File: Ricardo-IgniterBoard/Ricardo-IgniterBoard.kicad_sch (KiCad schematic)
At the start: 39 parts, among them J101 RBUS, U101 ESP32-S3, Y101 R940000171

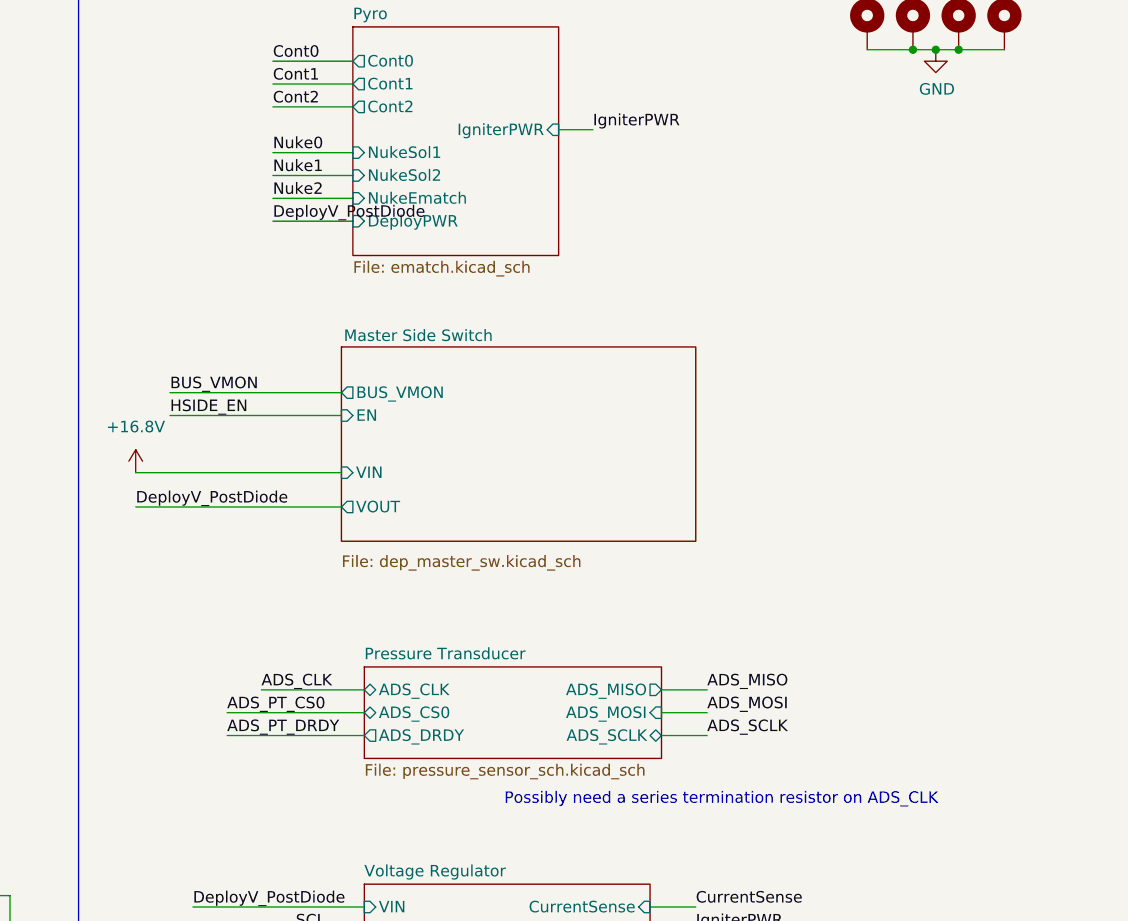
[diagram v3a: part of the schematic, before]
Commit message: some more changes
added current sensor for solenoid, fixed optocouplers
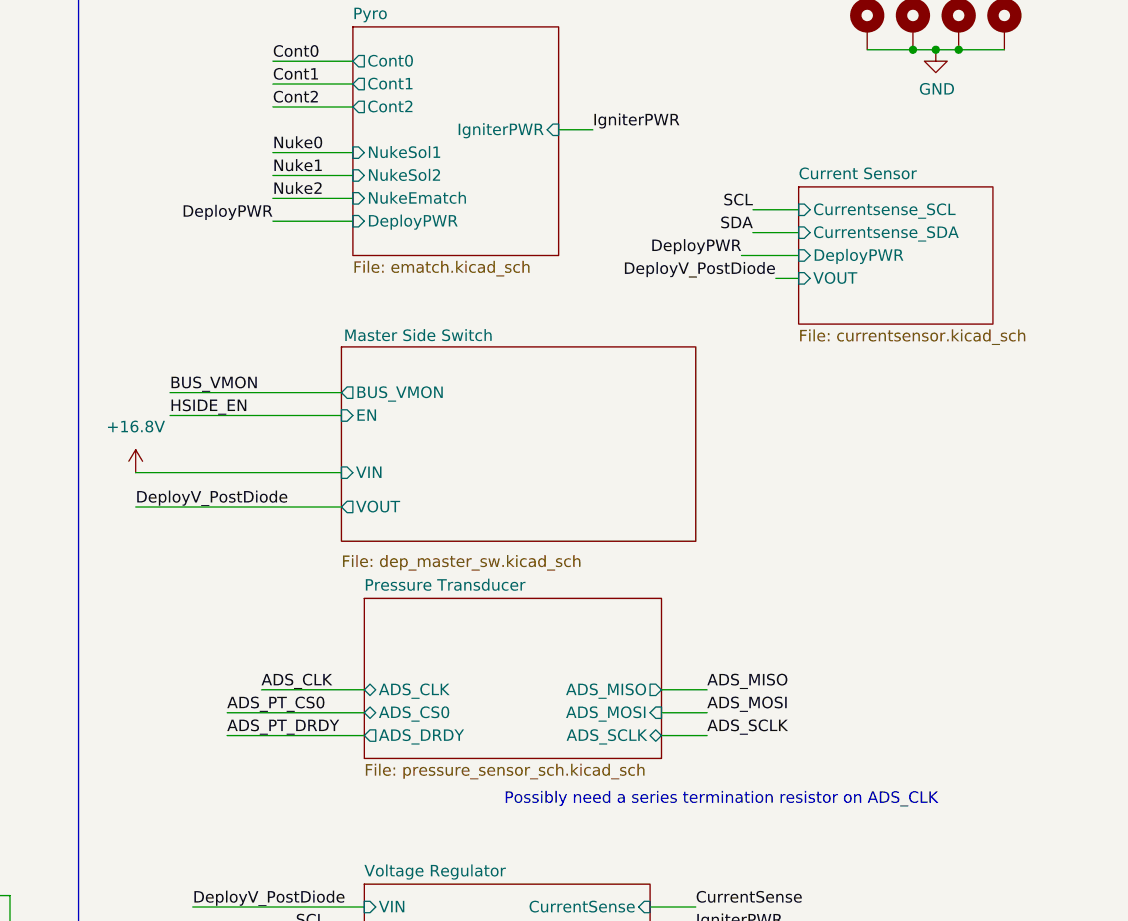
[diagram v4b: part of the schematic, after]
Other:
- added sheet Current Sensor (currentsensor.kicad_sch)
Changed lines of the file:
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@@
 	(wire
 		(pts
+			(xy 248.92 55.88) (xy 255.27 55.88)
+		)
+		(stroke
+			(width 0)
+			(type default)
+		)
+	)
+	(wire
+		(pts
 			(xy 69.85 135.89) (xy 69.85 138.43)
 		)
@@
 	(wire
 		(pts
+			(xy 250.19 50.8) (xy 255.27 50.8)
+		)
+		(stroke
+			(width 0)
+			(type default)
+		)
+	)
+	(wire
+		(pts
 			(xy 242.57 149.86) (xy 247.65 149.86)
 		)
@@
 	(wire
 		(pts
+			(xy 250.19 53.34) (xy 255.27 53.34)
+		)
+		(stroke
+			(width 0)
+			(type default)
+		)
+	)
+	(wire
+		(pts
 			(xy 196.85 46.99) (xy 205.74 46.99)
 		)
@@
 	(wire
 		(pts
+			(xy 252.73 58.42) (xy 255.27 58.42)
+		)
+		(stroke
+			(width 0)
+			(type default)
+		)
+	)
+	(wire
+		(pts
 			(xy 26.67 165.1) (xy 34.29 165.1)
 		)
@@
 		)
 	)
+	(label "DeployPWR"
+		(at 196.85 52.07 180)
+		(effects
+			(font
+				(size 1.27 1.27)
+			)
+			(justify right bottom)
+		)
+	)
 	(label "SDA"
 		(at 52.07 97.79 0)
@@
 		)
 	)
+	(label "SDA"
+		(at 250.19 53.34 180)
+		(effects
+			(font
+				(size 1.27 1.27)
+			)
+			(justify right bottom)
+		)
+	)
 	(label "Nuke2"
 		(at 196.85 49.53 0)
@@
 		)
 	)
+	(label "DeployPWR"
+		(at 248.92 55.88 180)
+		(effects
+			(font
+				(size 1.27 1.27)
+			)
+			(justify right bottom)
+		)
+	)
 	(label "ADS_PT_CS0"
 		(at 66.04 95.25 180)
@@
 		)
 	)
+	(label "DeployV_PostDiode"
+		(at 252.73 58.42 180)
+		(effects
+			(font
+				(size 1.27 1.27)
+			)
+			(justify right bottom)
+		)
+	)
 	(label "IgniterPWR"
 		(at 232.41 41.91 0)
@@
 		)
 	)
+	(label "SCL"
+		(at 250.19 50.8 180)
+		(effects
+			(font
+				(size 1.27 1.27)
+			)
+			(justify right bottom)
+		)
+	)
 	(label "ADS_MISO"
 		(at 245.11 104.14 0)
@@
 		)
 	)
-	(label "DeployV_PostDiode"
-		(at 196.85 52.07 0)
-		(effects
-			(font
-				(size 1.27 1.27)
-			)
-			(justify left bottom)
-		)
-	)
 	(label "Nuke1"
 		(at 138.43 97.79 0)
@@
 	)
 	(sheet
-		(at 207.01 101.6)
-		(size 33.02 10.16)
+		(at 255.27 48.26)
+		(size 21.59 15.24)
+		(exclude_from_sim no)
+		(in_bom yes)
+		(on_board yes)
+		(dnp no)
+		(fields_autoplaced yes)
+		(stroke
+			(width 0.1524)
+			(type solid)
+		)
+		(fill
+			(color 0 0 0 0.0000)
+		)
+		(property "Sheetname" "Current Sensor"
+			(at 255.27 47.5484 0)
+			(effects
+				(font
+					(size 1.27 1.27)
+				)
+				(justify left bottom)
+			)
+		)
+		(property "Sheetfile" "currentsensor.kicad_sch"
+			(at 255.27 64.0846 0)
+			(effects
+				(font
+					(size 1.27 1.27)
+				)
+				(justify left top)
+			)
+		)
+		(pin "Currentsense_SCL" input
+			(at 255.27 50.8 180)
+			(effects
+				(font
+					(size 1.27 1.27)
+				)
+				(justify left)
+			)
+		)
+		(pin "Currentsense_SDA" input
+			(at 255.27 53.34 180)
+			(effects
+				(font
+					(size 1.27 1.27)
+				)
+				(justify left)
+			)
+		)
+		(pin "DeployPWR" input
+			(at 255.27 55.88 180)
+			(effects
+				(font
+					(size 1.27 1.27)
+				)
+				(justify left)
+			)
+		)
+		(pin "VOUT" input
+			(at 255.27 58.42 180)
+			(effects
+				(font
+					(size 1.27 1.27)
+				)
+				(justify left)
+			)
+		)
+		(instances
+			(project "Ricardo-IgniterBoard"
+				(path "/7db990e4-92e1-4f99-b4d2-435bbec1ba83"
+					(page "10")
+				)
+			)
+		)
+	)
+	(sheet
+		(at 207.01 93.98)
+		(size 33.02 17.78)
 		(exclude_from_sim no)
 		(in_bom yes)
@@
 		)
 		(property "Sheetname" "Pressure Transducer"
-			(at 207.01 100.8884 0)
+			(at 207.01 93.2684 0)
 			(effects
 				(font
